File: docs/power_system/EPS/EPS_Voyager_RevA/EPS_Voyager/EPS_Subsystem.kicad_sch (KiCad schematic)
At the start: 42 parts, among them J1 Conn_01x02_Socket, J10 Conn_01x02_Socket, J11 Conn_01x02_Socket, J13 Conn_01x01_Socket, J3 Conn_01x02_Socket, J4 Conn_01x02_Socket, J5 Conn_01x02_Socket, J6 Conn_01x02_Socket, J7 Conn_01x02_Socket, J8 Conn_01x02_Socket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

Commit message: Small Revisions
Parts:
- removed R44: 25k, Resistor_SMD:R_0603_1608Metric, symbol Device:R
- removed R45: 5.5k, Resistor_SMD:R_0603_1608Metric, symbol Device:R
- added J17, J18: Conn_01x02_Socket, Connector_PinSocket_2.54mm:PinSocket_1x02_P2.54mm_Vertical, symbol Connector:Conn_01x02_Socket
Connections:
- net GND: now also J17.2 (Pin_2)
- net at C28.1, C29.1, C30.1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: now also J18.1 (Pin_1)
- net at C28.2, U5.28 (FB): now also J17.1 (Pin_1), J18.2 (Pin_2)
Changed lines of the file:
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@@
 	)
 	(junction
+		(at 186.69 60.96)
+		(diameter 0)
+		(color 0 0 0 0)
+	)
+	(junction
 		(at 152.4 35.56)
 		(diameter 0)
@@
 	)
 	(junction
-		(at 224.79 67.31)
+		(at 186.69 68.58)
 		(diameter 0)
 		(color 0 0 0 0)
 	)
 	(junction
-		(at 99.06 52.07)
+		(at 224.79 67.31)
 		(diameter 0)
 		(color 0 0 0 0)
 	)
 	(junction
-		(at 186.69 68.58)
+		(at 99.06 52.07)
 		(diameter 0)
 		(color 0 0 0 0)
@@
 	)
 	(junction
-		(at 186.69 60.96)
-		(diameter 0)
-		(color 0 0 0 0)
-	)
-	(junction
 		(at 124.46 39.37)
 		(diameter 0)
@@
 	(wire
 		(pts
+			(xy 186.69 73.66) (xy 186.69 77.47)
+		)
+		(stroke
+			(width 0)
+			(type default)
+		)
+	)
+	(wire
+		(pts
 			(xy 157.48 40.64) (xy 157.48 38.1)
 		)
@@
 	(wire
 		(pts
+			(xy 186.69 60.96) (xy 186.69 63.5)
+		)
+		(stroke
+			(width 0)
+			(type default)
+		)
+	)
+	(wire
+		(pts
 			(xy 147.32 40.64) (xy 147.32 34.29)
 		)
@@
 	(wire
 		(pts
+			(xy 186.69 66.04) (xy 186.69 68.58)
+		)
+		(stroke
+			(width 0)
+			(type default)
+		)
+	)
+	(wire
+		(pts
 			(xy 175.26 68.58) (xy 186.69 68.58)
 		)
@@
 	(wire
 		(pts
-			(xy 186.69 77.47) (xy 186.69 76.2)
-		)
-		(stroke
-			(width 0)
-			(type default)
-		)
-	)
-	(wire
-		(pts
 			(xy 38.1 88.9) (xy 38.1 92.71)
 		)
@@
 	(wire
 		(pts
+			(xy 186.69 68.58) (xy 186.69 71.12)
+		)
+		(stroke
+			(width 0)
+			(type default)
+		)
+	)
+	(wire
+		(pts
 			(xy 109.22 52.07) (xy 115.57 52.07)
 		)
@@
 	)
 	(symbol
+		(lib_id "Connector:Conn_01x02_Socket")
+		(at 191.77 71.12 0)
+		(unit 1)
+		(exclude_from_sim no)
+		(in_bom yes)
+		(on_board yes)
+		(dnp no)
+		(property "Reference" "J17"
+			(at 189.992 75.692 0)
+			(effects
+				(font
+					(size 1.27 1.27)
+				)
+			)
+		)
+		(property "Value" "Conn_01x02_Socket"
+			(at 191.135 76.2 0)
+			(effects
+				(font
+					(size 1.27 1.27)
+				)
+				(hide yes)
+			)
+		)
+		(property "Footprint" "Connector_PinSocket_2.54mm:PinSocket_1x02_P2.54mm_Vertical"
+			(at 191.77 71.12 0)
+			(effects
+				(font
+					(size 1.27 1.27)
+				)
+				(hide yes)
+			)
+		)
+		(property "Datasheet" "~"
+			(at 191.77 71.12 0)
+			(effects
+				(font
+					(size 1.27 1.27)
+				)
+				(hide yes)
+			)
+		)
+		(property "Description" "Generic connector, single row, 01x02, script generated"
+			(at 191.77 71.12 0)
+			(effects
+				(font
+					(size 1.27 1.27)
+				)
+				(hide yes)
+			)
+		)
+		(pin "1"
+		)
+		(pin "2"
+		)
+		(instances
+			(project "EPS_Voyager"
+				(path "/9e935f60-3970-4544-bfdc-c9319d9d6774/0762457c-a6e3-46eb-8072-fdbc6a260216"
+					(reference "J17")
+					(unit 1)
+				)
+			)
+		)
+	)
+	(symbol
 		(lib_id "Device:C")
 		(at 234.95 62.23 270)
@@
 	)
 	(symbol
-		(lib_id "Device:R")
-		(at 186.69 72.39 0)
-		(unit 1)
-		(exclude_from_sim no)
-		(in_bom yes)
-		(on_board yes)
-		(dnp no)
-		(property "Reference" "R45"
-			(at 190.246 72.898 0)
-			(effects
-				(font
-					(size 1.27 1.27)
-				)
-			)
-		)
-		(property "Value" "5.5k"
-			(at 190.5 70.866 0)
-			(effects
-				(font
-					(size 1.27 1.27)
-				)
-			)
-		)
-		(property "Footprint" "Resistor_SMD:R_0603_1608Metric"
-			(at 184.912 72.39 90)
-			(effects
-				(font
-					(size 1.27 1.27)
-				)
-				(hide yes)
-			)
-		)
-		(property "Datasheet" "~"
-			(at 186.69 72.39 0)
-			(effects
-				(font
-					(size 1.27 1.27)
-				)
-				(hide yes)
-			)
-		)
-		(property "Description" "Resistor"
-			(at 186.69 72.39 0)
-			(effects
-				(font
-					(size 1.27 1.27)
-				)
-				(hide yes)
-			)
-		)
-		(pin "2"
-		)
-		(pin "1"
-		)
-		(instances
-			(project "EPS_Voyager"
-				(path "/9e935f60-3970-4544-bfdc-c9319d9d6774/0762457c-a6e3-46eb-8072-fdbc6a260216"
-					(reference "R45")
-					(unit 1)
-				)
-			)
-		)
-	)
-	(symbol
 		(lib_id "power:PWR_FLAG")
 		(at 224.79 69.85 90)
@@
 	)
 	(symbol
+		(lib_id "Connector:Conn_01x02_Socket")
+		(at 191.77 63.5 0)
+		(unit 1)
+		(exclude_from_sim no)
+		(in_bom yes)
+		(on_board yes)
+		(dnp no)
+		(property "Reference" "J18"
+			(at 189.992 68.072 0)
+			(effects
+				(font
+					(size 1.27 1.27)
+				)
+			)
+		)
+		(property "Value" "Conn_01x02_Socket"
+			(at 191.135 68.58 0)
+			(effects
+				(font
+					(size 1.27 1.27)
+				)
+				(hide yes)
+			)
+		)
+		(property "Footprint" "Connector_PinSocket_2.54mm:PinSocket_1x02_P2.54mm_Vertical"
+			(at 191.77 63.5 0)
+			(effects
+				(font
+					(size 1.27 1.27)
+				)
+				(hide yes)
+			)
+		)
+		(property "Datasheet" "~"
+			(at 191.77 63.5 0)
+			(effects
+				(font
+					(size 1.27 1.27)
+				)
+				(hide yes)
+			)
+		)
+		(property "Description" "Generic connector, single row, 01x02, script generated"
+			(at 191.77 63.5 0)
+			(effects
+				(font
+					(size 1.27 1.27)
+				)
+				(hide yes)
+			)
+		)
+		(pin "1"
+		)
+		(pin "2"
+		)
+		(instances
+			(project "EPS_Voyager"
+				(path "/9e935f60-3970-4544-bfdc-c9319d9d6774/0762457c-a6e3-46eb-8072-fdbc6a260216"
+					(reference "J18")
+					(unit 1)
+				)
+			)
+		)
+	)
+	(symbol
 		(lib_id "Connector:TestPoint")
 		(at 100.33 30.48 0)
@@
 					(unit 1)
 				)
-			)
-		)
-	)
-	(symbol
-		(lib_id "Device:R")
-		(at 186.69 64.77 180)
-		(unit 1)
-		(exclude_from_sim no)
-		(in_bom yes)
-		(on_board yes)
-		(dnp no)
-		(property "Reference" "R44"
-			(at 190.5 64.516 0)
-			(effects
-				(font
-					(size 1.27 1.27)
-				)
-			)
-		)
-		(property "Value" "25k"
-			(at 190.5 62.738 0)
-			(effects
-				(font
-					(size 1.27 1.27)
-				)
-			)
-		)
-		(property "Footprint" "Resistor_SMD:R_0603_1608Metric"
-			(at 188.468 64.77 90)
-			(effects
-				(font
-					(size 1.27 1.27)
-				)
-				(hide yes)
-			)
-		)
-		(property "Datasheet" "~"
-			(at 186.69 64.77 0)
-			(effects
-				(font
-					(size 1.27 1.27)
-				)
-				(hide yes)
-			)
-		)
-		(property "Description" "Resistor"
-			(at 186.69 64.77 0)
-			(effects
-				(font
-					(size 1.27 1.27)
-				)
-				(hide yes)
-			)
-		)
-		(pin "2"
-		)
-		(pin "1"
-		)
-		(instances
-			(project "EPS_Voyager"
-				(path "/9e935f60-3970-4544-bfdc-c9319d9d6774/0762457c-a6e3-46eb-8072-fdbc6a260216"
-					(reference "R44")
-					(unit 1)
-				)

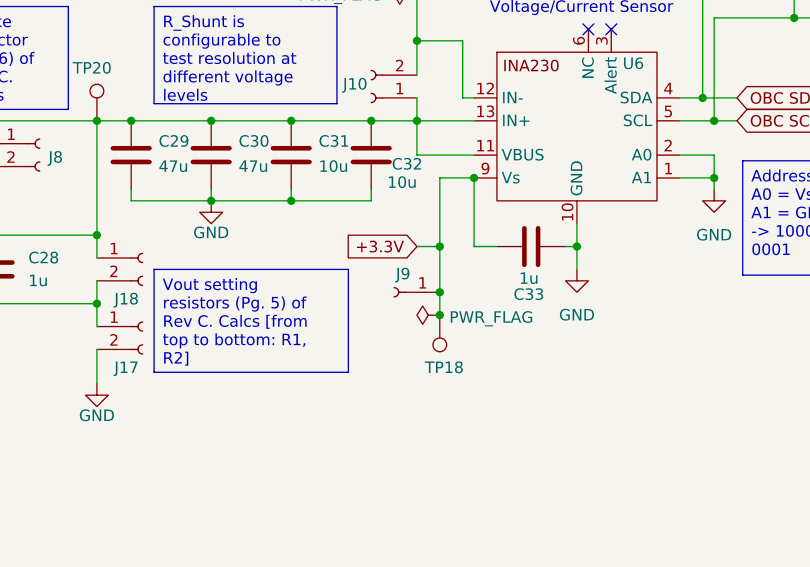
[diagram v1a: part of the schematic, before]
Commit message: WD Testing and Minor Schematic Updates to EPS Voyager
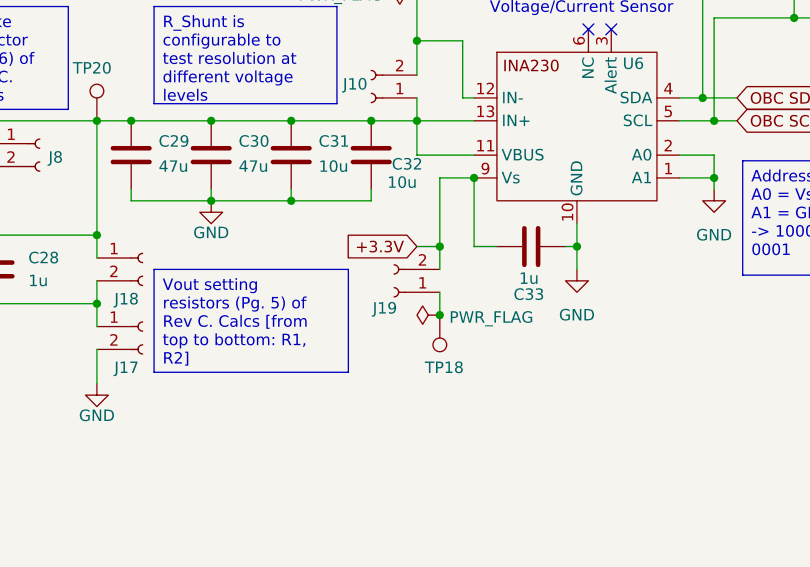
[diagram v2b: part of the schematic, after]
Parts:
- removed J9: Conn_01x01_Socket, Connector_PinSocket_2.54mm:PinSocket_1x02_P2.54mm_Vertical, symbol Connector:Conn_01x01_Socket
- added J19: Conn_01x02_Socket, Connector_PinSocket_2.54mm:PinSocket_1x02_P2.54mm_Vertical, symbol Connector:Conn_01x02_Socket
- J12: footprint RevC Footprints:SISB46DN-T1-GE3 -> REVC:SISB46DN-T1-GE3
- U4: footprint RevC Footprints:LTC4365 -> REVC:LTC4365
- U5: footprint RevC Footprints:LT8638SEVPBF -> REVC:LT8638SEVPBF
- U6: footprint RevC Footprints:INA230AIRGTT -> REVC:INA230AIRGTT
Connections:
- net +3.3V: now also J19.2 (Pin_2); no longer TP18.1
- new net: J19.1 (Pin_1), TP18.1
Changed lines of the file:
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@@
 	)
 	(junction
-		(at 224.79 67.31)
-		(diameter 0)
-		(color 0 0 0 0)
-	)
-	(junction
 		(at 99.06 52.07)
 		(diameter 0)
@@
 	(wire
 		(pts
-			(xy 224.79 69.85) (xy 224.79 67.31)
+			(xy 224.79 62.23) (xy 224.79 64.77)
 		)
 		(stroke
@@
 	(wire
 		(pts
-			(xy 224.79 67.31) (xy 224.79 62.23)
-		)
-		(stroke
-			(width 0)
-			(type default)
-		)
-	)
-	(wire
-		(pts
 			(xy 186.69 60.96) (xy 186.69 63.5)
 		)
@@
 	(wire
 		(pts
+			(xy 224.79 67.31) (xy 224.79 69.85)
+		)
+		(stroke
+			(width 0)
+			(type default)
+		)
+	)
+	(wire
+		(pts
 			(xy 109.22 62.23) (xy 128.27 62.23)
 		)
@@
 			)
 		)
-		(property "Footprint" "RevC Footprints:LT8638SEVPBF"
+		(property "Footprint" "REVC:LT8638SEVPBF"
 			(at 144.78 58.42 0)
 			(effects
@@
 	)
 	(symbol
-		(lib_id "Connector:Conn_01x01_Socket")
-		(at 219.71 67.31 180)
-		(unit 1)
-		(exclude_from_sim no)
-		(in_bom yes)
-		(on_board yes)
-		(dnp no)
-		(property "Reference" "J9"
-			(at 220.726 65.278 0)
-			(effects
-				(font
-					(size 1.27 1.27)
-				)
-			)
-		)
-		(property "Value" "Conn_01x01_Socket"
-			(at 220.345 64.77 0)
-			(effects
-				(font
-					(size 1.27 1.27)
-				)
-				(hide yes)
-			)
-		)
-		(property "Footprint" "Connector_PinSocket_2.54mm:PinSocket_1x02_P2.54mm_Vertical"
-			(at 219.71 67.31 0)
-			(effects
-				(font
-					(size 1.27 1.27)
-				)
-				(hide yes)
-			)
-		)
-		(property "Datasheet" "~"
-			(at 219.71 67.31 0)
-			(effects
-				(font
-					(size 1.27 1.27)
-				)
-				(hide yes)
-			)
-		)
-		(property "Description" "Generic connector, single row, 01x01, script generated"
-			(at 219.71 67.31 0)
-			(effects
-				(font
-					(size 1.27 1.27)
-				)
-				(hide yes)
-			)
-		)
-		(pin "1"
-		)
-		(instances
-			(project ""
-				(path "/9e935f60-3970-4544-bfdc-c9319d9d6774/0762457c-a6e3-46eb-8072-fdbc6a260216"
-					(reference "J9")
-					(unit 1)
-				)
-			)
-		)
-	)
-	(symbol
 		(lib_id "SISB46DN:SISB46DN")
 		(at 87.63 31.75 0)
@@
 			)
 		)
-		(property "Footprint" "RevC Footprints:SISB46DN-T1-GE3"
+		(property "Footprint" "REVC:SISB46DN-T1-GE3"
 			(at 87.63 31.75 0)
 			(effects
@@
 			)
 		)
-		(property "Footprint" "RevC Footprints:LTC4365"
+		(property "Footprint" "REVC:LTC4365"
 			(at 86.36 55.88 0)
 			(effects
@@
 			)
 		)
-		(property "Footprint" "RevC Footprints:INA230AIRGTT"
+		(property "Footprint" "REVC:INA230AIRGTT"
 			(at 240.03 49.53 0)
 			(effects
@@
 					(unit 1)
 				)
+			)
+		)
+	)
+	(symbol
+		(lib_id "Connector:Conn_01x02_Socket")
+		(at 219.71 67.31 180)
+		(unit 1)
+		(exclude_from_sim no)
+		(in_bom yes)
+		(on_board yes)
+		(dnp no)
+		(property "Reference" "J19"
+			(at 218.694 69.088 0)
+			(effects
+				(font
+					(size 1.27 1.27)
+				)
+			)
+		)
+		(property "Value" "Conn_01x02_Socket"
+			(at 220.345 62.23 0)
+			(effects
+				(font
+					(size 1.27 1.27)
+				)
+				(hide yes)
+			)
+		)
+		(property "Footprint" "Connector_PinSocket_2.54mm:PinSocket_1x02_P2.54mm_Vertical"
+			(at 219.71 67.31 0)
+			(effects
+				(font
+					(size 1.27 1.27)
+				)
+				(hide yes)
+			)
+		)
+		(property "Datasheet" "~"
+			(at 219.71 67.31 0)
+			(effects
+				(font
+					(size 1.27 1.27)
+				)
+				(hide yes)
+			)
+		)
+		(property "Description" "Generic connector, single row, 01x02, script generated"
+			(at 219.71 67.31 0)
+			(effects
+				(font
+					(size 1.27 1.27)
+				)
+				(hide yes)
+			)
+		)
+		(pin "1"
+		)
+		(pin "2"
+		)
+		(instances
+			(project "EPS_Voyager"
+				(path "/9e935f60-3970-4544-bfdc-c9319d9d6774/0762457c-a6e3-46eb-8072-fdbc6a260216"
+					(reference "J19")
+					(unit 1)
+				)

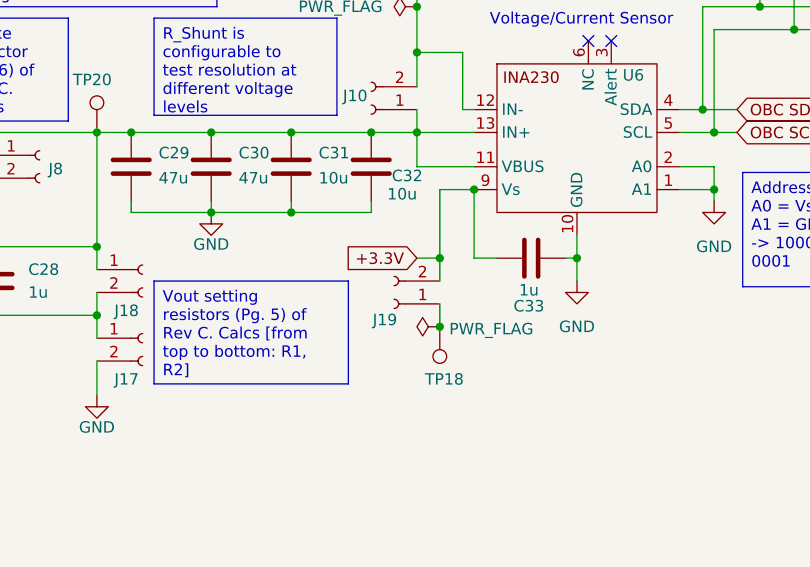
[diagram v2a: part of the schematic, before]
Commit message: Organized Voyager layout
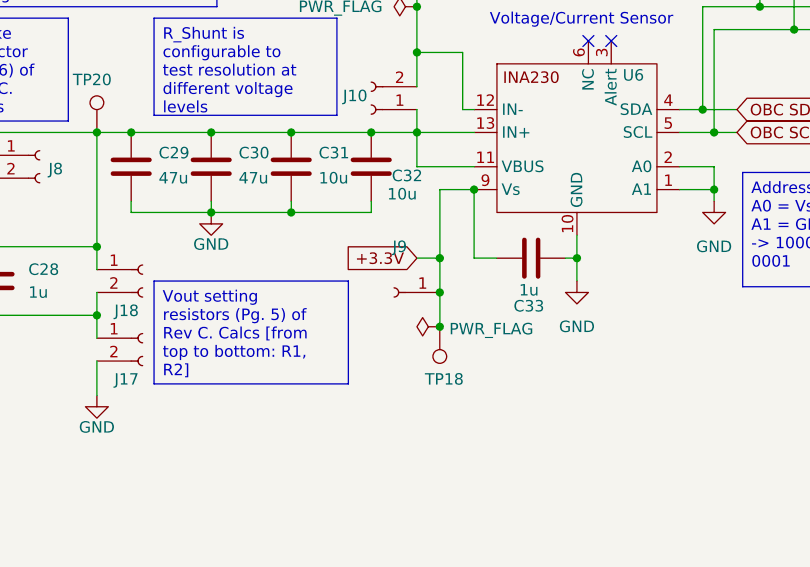
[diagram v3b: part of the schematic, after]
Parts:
- removed J19: Conn_01x02_Socket, Connector_PinSocket_2.54mm:PinSocket_1x02_P2.54mm_Vertical, symbol Connector:Conn_01x02_Socket
- added J9: Conn_01x01_Socket, Connector_PinSocket_2.54mm:PinSocket_1x01_P2.54mm_Vertical, symbol Connector:Conn_01x01_Socket
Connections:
- net +3.3V: now also TP18.1, J9.1 (Pin_1)
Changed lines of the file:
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@@
 	)
 	(junction
+		(at 224.79 66.04)
+		(diameter 0)
+		(color 0 0 0 0)
+	)
+	(junction
 		(at 255.27 54.61)
 		(diameter 0)
@@
 	(wire
 		(pts
-			(xy 224.79 62.23) (xy 224.79 64.77)
-		)
-		(stroke
-			(width 0)
-			(type default)
-		)
-	)
-	(wire
-		(pts
 			(xy 255.27 36.83) (xy 264.16 36.83)
 		)
@@
 	(wire
 		(pts
+			(xy 224.79 62.23) (xy 224.79 66.04)
+		)
+		(stroke
+			(width 0)
+			(type default)
+		)
+	)
+	(wire
+		(pts
 			(xy 152.4 30.48) (xy 152.4 35.56)
 		)
@@
 	(wire
 		(pts
+			(xy 224.79 66.04) (xy 224.79 69.85)
+		)
+		(stroke
+			(width 0)
+			(type default)
+		)
+	)
+	(wire
+		(pts
 			(xy 255.27 48.26) (xy 255.27 36.83)
 		)
@@
 	(wire
 		(pts
-			(xy 224.79 67.31) (xy 224.79 69.85)
-		)
-		(stroke
-			(width 0)
-			(type default)
-		)
-	)
-	(wire
-		(pts
 			(xy 109.22 62.23) (xy 128.27 62.23)
 		)
@@
 	)
 	(symbol
+		(lib_id "Connector:Conn_01x01_Socket")
+		(at 219.71 66.04 180)
+		(unit 1)
+		(exclude_from_sim no)
+		(in_bom yes)
+		(on_board yes)
+		(dnp no)
+		(fields_autoplaced yes)
+		(property "Reference" "J9"
+			(at 220.345 60.96 0)
+			(effects
+				(font
+					(size 1.27 1.27)
+				)
+			)
+		)
+		(property "Value" "Conn_01x01_Socket"
+			(at 220.345 63.5 0)
+			(effects
+				(font
+					(size 1.27 1.27)
+				)
+				(hide yes)
+			)
+		)
+		(property "Footprint" "Connector_PinSocket_2.54mm:PinSocket_1x01_P2.54mm_Vertical"
+			(at 219.71 66.04 0)
+			(effects
+				(font
+					(size 1.27 1.27)
+				)
+				(hide yes)
+			)
+		)
+		(property "Datasheet" "~"
+			(at 219.71 66.04 0)
+			(effects
+				(font
+					(size 1.27 1.27)
+				)
+				(hide yes)
+			)
+		)
+		(property "Description" "Generic connector, single row, 01x01, script generated"
+			(at 219.71 66.04 0)
+			(effects
+				(font
+					(size 1.27 1.27)
+				)
+				(hide yes)
+			)
+		)
+		(pin "1"
+		)
+		(instances
+			(project ""
+				(path "/9e935f60-3970-4544-bfdc-c9319d9d6774/0762457c-a6e3-46eb-8072-fdbc6a260216"
+					(reference "J9")
+					(unit 1)
+				)
+			)
+		)
+	)
+	(symbol
 		(lib_id "power:GND")
 		(at 109.22 72.39 0)
@@
 					(unit 1)
 				)
-			)
-		)
-	)
-	(symbol
-		(lib_id "Connector:Conn_01x02_Socket")
-		(at 219.71 67.31 180)
-		(unit 1)
-		(exclude_from_sim no)
-		(in_bom yes)
-		(on_board yes)
-		(dnp no)
-		(property "Reference" "J19"
-			(at 218.694 69.088 0)
-			(effects
-				(font
-					(size 1.27 1.27)
-				)
-			)
-		)
-		(property "Value" "Conn_01x02_Socket"
-			(at 220.345 62.23 0)
-			(effects
-				(font
-					(size 1.27 1.27)
-				)
-				(hide yes)
-			)
-		)
-		(property "Footprint" "Connector_PinSocket_2.54mm:PinSocket_1x02_P2.54mm_Vertical"
-			(at 219.71 67.31 0)
-			(effects
-				(font
-					(size 1.27 1.27)
-				)
-				(hide yes)
-			)
-		)
-		(property "Datasheet" "~"
-			(at 219.71 67.31 0)
-			(effects
-				(font
-					(size 1.27 1.27)
-				)
-				(hide yes)
-			)
-		)
-		(property "Description" "Generic connector, single row, 01x02, script generated"
-			(at 219.71 67.31 0)
-			(effects
-				(font
-					(size 1.27 1.27)
-				)
-				(hide yes)
-			)
-		)
-		(pin "1"
-		)
-		(pin "2"
-		)
-		(instances
-			(project "EPS_Voyager"
-				(path "/9e935f60-3970-4544-bfdc-c9319d9d6774/0762457c-a6e3-46eb-8072-fdbc6a260216"
-					(reference "J19")
-					(unit 1)
-				)
